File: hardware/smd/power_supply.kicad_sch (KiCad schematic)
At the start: 29 parts, among them T1 Wurth 750370423, U1 LM1117IMPX-3.3, U2 VIPER06, U3 EL3H7, U4 TL431

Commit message: Add capacitor specifications, change capacity around crystal
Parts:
- C10, C2, C6: value 100n 10V -> 100n 10V X7R
- C11: value 100n 35V -> 100n 35V X7R
- C12: value 1n 10V -> 1n 10V X7R
- C13: value 2.2n 35V -> 2.2n 35V X7R
- C7: value 2.2n 50V -> 2.2n 50V X7R
- renumbered C5 to C4, C4 to C5
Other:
- moved on the sheet: C12, C13, C5, C6, R2, R3, R4, U1, U3, U4

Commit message: Drop all tht legacy footprints
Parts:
- C1, C5: footprint KiCadX_Capacitors_THT:CP_Radial_D5.0mm_P1.50mm -> (none)
- C10, C11, C13, C7: footprint Capacitor_THT:C_Disc_D6.0mm_W2.5mm_P5.00mm -> (none)
- C12: footprint Capacitor_THT:C_Disc_D4.3mm_W1.9mm_P5.00mm -> (none)
- C2, C6: footprint Capacitor_THT:C_Disc_D5.0mm_W2.5mm_P5.00mm -> (none)
- C3: footprint Capacitor_THT:C_Rect_L26.5mm_W5.0mm_P22.50mm_MKS4 -> (none)
- D1: footprint Diode_THT:Diode_Bridge_DIP-4_W7.62mm_P5.08mm -> (none)
- D2, D3: footprint Diode_THT:D_DO-41_SOD81_P10.16mm_Horizontal -> (none)
- F1: footprint KiCadX_FuseHolders_THT:FuseHolder_THT_5x20mm_PTF76_RM15mm -> (none)
- R2, R3, R4: footprint Resistor_THT:R_Axial_DIN0207_L6.3mm_D2.5mm_P7.62mm_Horizontal -> (none)
- RV1: footprint Varistor:RV_Disc_D9mm_W3.4mm_P5mm -> (none)
- U1: footprint Package_TO_SOT_SMD:SOT-223-3_TabPin2 -> (none)
- U3: footprint Package_DIP:DIP-4_W7.62mm -> (none)
- U4: footprint Package_TO_SOT_SMD:SOT-23 -> (none)
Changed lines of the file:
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@@
 			)
 		)
-		(property "Footprint" "Capacitor_THT:C_Disc_D5.0mm_W2.5mm_P5.00mm"
+		(property "Footprint" ""
 			(at 113.9952 132.08 0)
 			(effects
@@
 			)
 		)
-		(property "Footprint" "Resistor_THT:R_Axial_DIN0207_L6.3mm_D2.5mm_P7.62mm_Horizontal"
+		(property "Footprint" ""
 			(at 172.72 79.248 90)
 			(effects
@@
 			)
 		)
-		(property "Footprint" "Capacitor_THT:C_Rect_L26.5mm_W5.0mm_P22.50mm_MKS4"
+		(property "Footprint" ""
 			(at 80.9752 66.04 0)
 			(effects
@@
 			)
 		)
-		(property "Footprint" "Resistor_THT:R_Axial_DIN0207_L6.3mm_D2.5mm_P7.62mm_Horizontal"
+		(property "Footprint" ""
 			(at 177.292 88.9 90)
 			(effects
@@
 			)
 		)
-		(property "Footprint" "Capacitor_THT:C_Disc_D5.0mm_W2.5mm_P5.00mm"
+		(property "Footprint" ""
 			(at 60.6552 132.08 0)
 			(effects
@@
 			)
 		)
-		(property "Footprint" "Capacitor_THT:C_Disc_D4.3mm_W1.9mm_P5.00mm"
+		(property "Footprint" ""
 			(at 172.4152 46.99 0)
 			(effects
@@
 			)
 		)
-		(property "Footprint" "Package_TO_SOT_SMD:SOT-223-3_TabPin2"
+		(property "Footprint" ""
 			(at 85.09 124.46 0)
 			(effects
@@
 			)
 		)
-		(property "Footprint" "KiCadX_Capacitors_THT:CP_Radial_D5.0mm_P1.50mm"
+		(property "Footprint" ""
 			(at 97.4852 132.08 0)
 			(effects
@@
 			)
 		)
-		(property "Footprint" "Diode_THT:D_DO-41_SOD81_P10.16mm_Horizontal"
+		(property "Footprint" ""
 			(at 133.35 55.88 0)
 			(effects
@@
 			)
 		)
-		(property "Footprint" "Diode_THT:D_DO-41_SOD81_P10.16mm_Horizontal"
+		(property "Footprint" ""
 			(at 128.27 39.37 0)
 			(effects
@@
 			)
 		)
-		(property "Footprint" "KiCadX_Capacitors_THT:CP_Radial_D5.0mm_P1.50mm"
+		(property "Footprint" ""
 			(at 44.1452 132.08 0)
 			(effects
@@
 			)
 		)
-		(property "Footprint" "Package_TO_SOT_SMD:SOT-23"
+		(property "Footprint" ""
 			(at 172.72 97.536 0)
 			(effects
@@
 			)
 		)
-		(property "Footprint" "Package_DIP:DIP-4_W7.62mm"
+		(property "Footprint" ""
 			(at 163.83 90.17 0)
 			(effects
@@
 			)
 		)
-		(property "Footprint" "Capacitor_THT:C_Disc_D6.0mm_W2.5mm_P5.00mm"
+		(property "Footprint" ""
 			(at 150.8252 46.99 0)
 			(effects
@@
 			)
 		)
-		(property "Footprint" "Capacitor_THT:C_Disc_D6.0mm_W2.5mm_P5.00mm"
+		(property "Footprint" ""
 			(at 133.0452 91.44 0)
 			(effects
@@
 			)
 		)
-		(property "Footprint" "Diode_THT:Diode_Bridge_DIP-4_W7.62mm_P5.08mm"
+		(property "Footprint" ""
 			(at 96.52 73.025 0)
 			(effects
@@
 			)
 		)
-		(property "Footprint" "Resistor_THT:R_Axial_DIN0207_L6.3mm_D2.5mm_P7.62mm_Horizontal"
+		(property "Footprint" ""
 			(at 177.292 81.28 90)
 			(effects
@@
 			)
 		)
-		(property "Footprint" "Capacitor_THT:C_Disc_D6.0mm_W2.5mm_P5.00mm"
+		(property "Footprint" ""
 			(at 172.4152 67.31 0)
 			(effects
@@
 			)
 		)
-		(property "Footprint" "Capacitor_THT:C_Disc_D6.0mm_W2.5mm_P5.00mm"
+		(property "Footprint" ""
 			(at 150.8252 67.31 0)
 			(effects
@@
 			)
 		)
-		(property "Footprint" "Varistor:RV_Disc_D9mm_W3.4mm_P5mm"
+		(property "Footprint" ""
 			(at 47.752 62.23 90)
 			(effects
@@
 			)
 		)
-		(property "Footprint" "KiCadX_FuseHolders_THT:FuseHolder_THT_5x20mm_PTF76_RM15mm"
+		(property "Footprint" ""
 			(at 43.18 57.658 90)
 			(effects

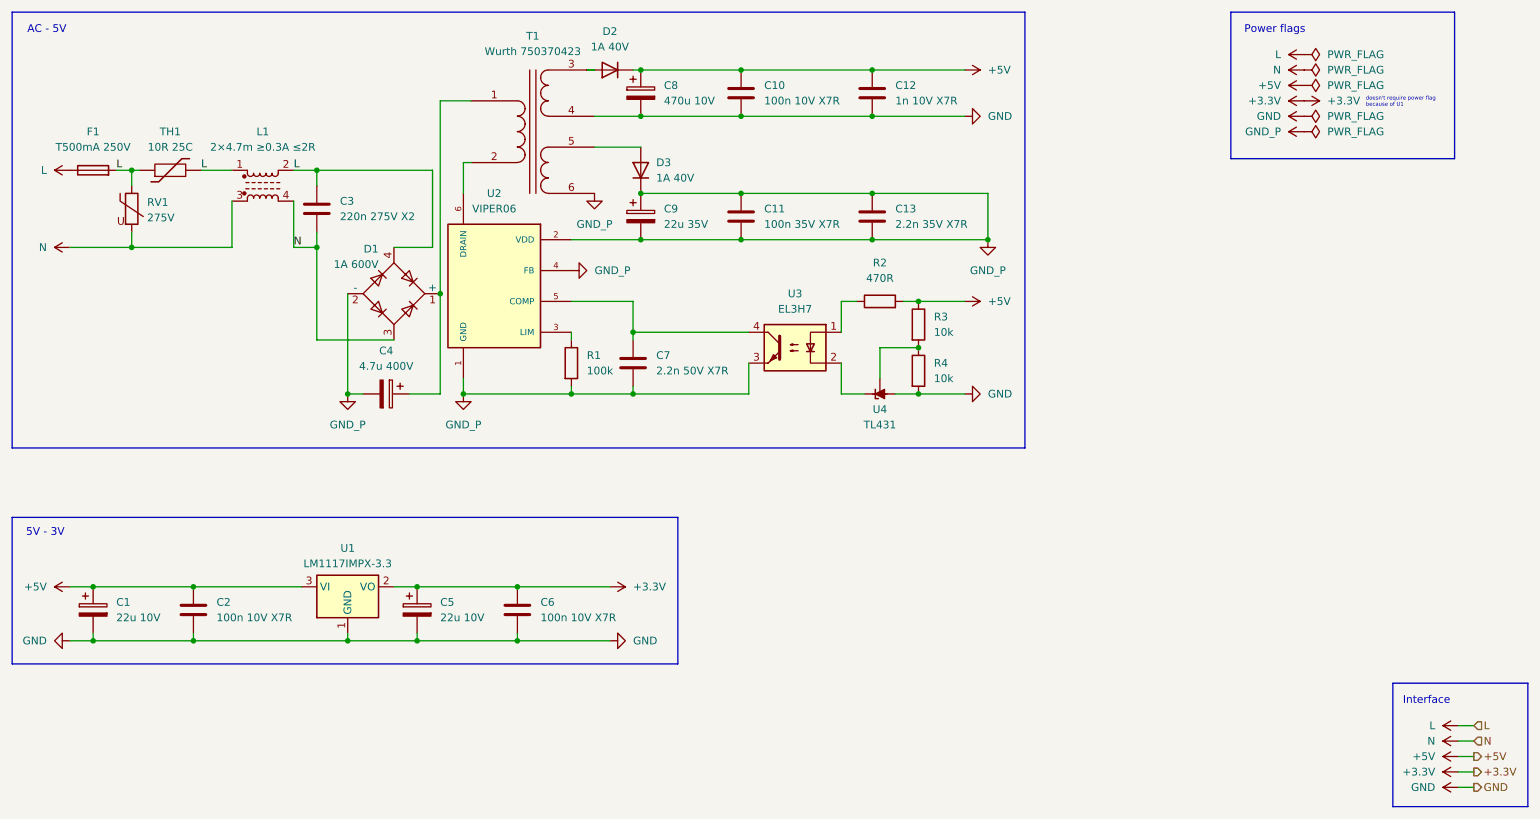
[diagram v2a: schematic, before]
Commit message: Assign footprints and JLC numbers (plus minor changes)
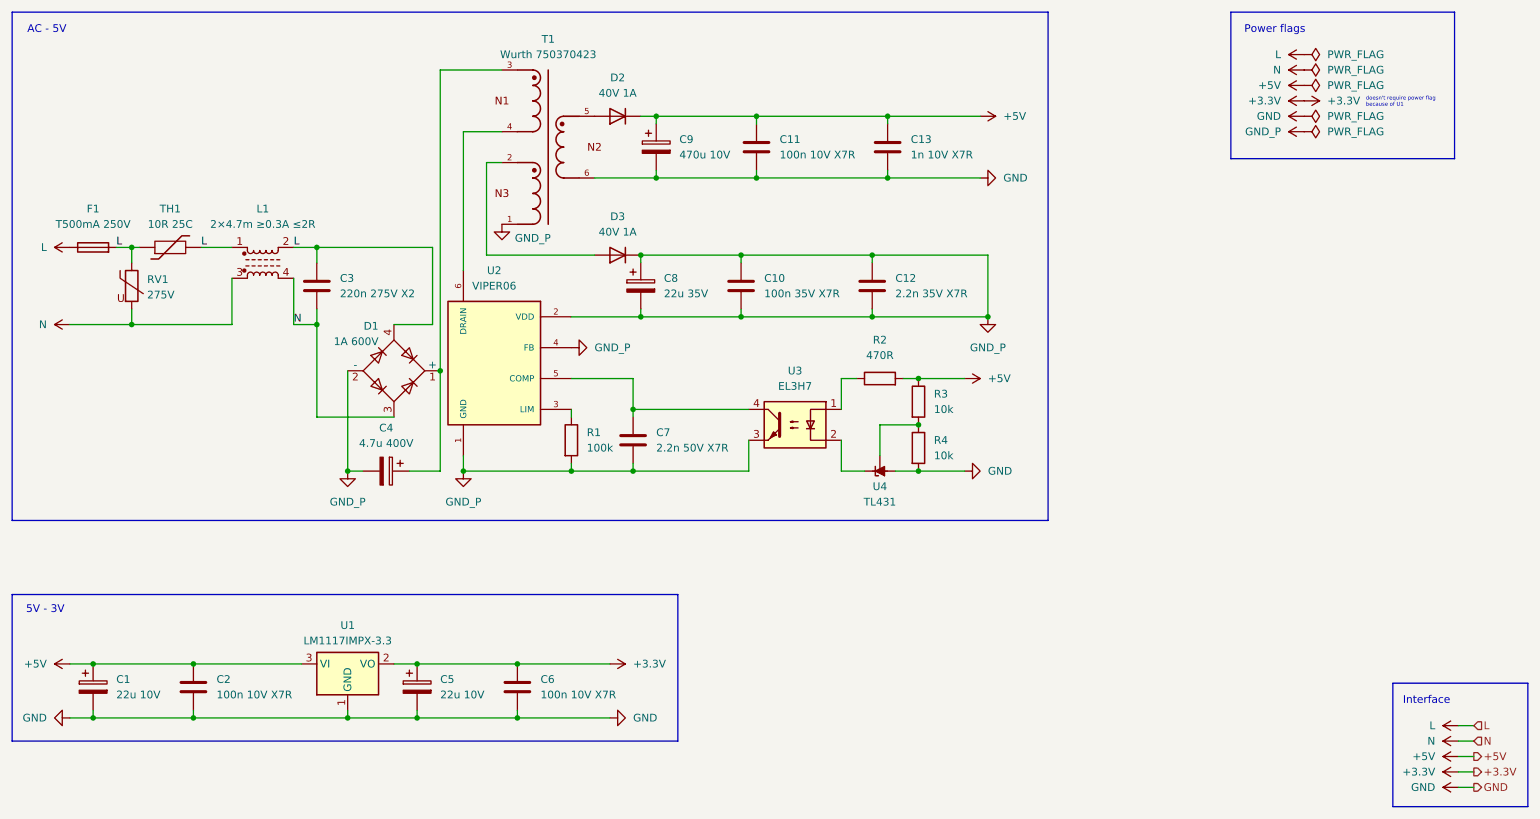
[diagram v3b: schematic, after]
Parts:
- removed T1: Wurth 750370423, symbol Device:Transformer_1P_2S
- added T1: Wurth 750370423, KiCadX_Transformers_THT:Wurth_750370423_THT_E13, symbol KiCadX_Transformers:Wurth_750370423
- C1, C5: footprint (none) -> Capacitor_SMD:CP_Elec_5x5.4; JLCPCB (none) -> C22387966
- C10: renamed from C11; footprint (none) -> Capacitor_SMD:C_0603_1608Metric; JLCPCB (none) -> C14663
- C11: renamed from C10; footprint (none) -> Capacitor_SMD:C_0402_1005Metric; JLCPCB (none) -> C309458
- C12: renamed from C13; footprint (none) -> Capacitor_SMD:C_0402_1005Metric; JLCPCB (none) -> C106861
- C13: renamed from C12; footprint (none) -> Capacitor_SMD:C_0402_1005Metric; JLCPCB (none) -> C541372
- C2, C6: footprint (none) -> Capacitor_SMD:C_0402_1005Metric; JLCPCB (none) -> C309458
- C3: footprint (none) -> Capacitor_THT:C_Rect_L13.0mm_W6.0mm_P10.00mm_FKS3_FKP3_MKS4; JLCPCB (none) -> C489075
- C4: footprint (none) -> Capacitor_SMD:CP_Elec_10x10.5; JLCPCB (none) -> C88703
- C7: footprint (none) -> Capacitor_SMD:C_0402_1005Metric; JLCPCB (none) -> C106861
- C8: renamed from C9; footprint (none) -> Capacitor_SMD:CP_Elec_5x5.4; JLCPCB (none) -> C239256
- C9: renamed from C8; footprint (none) -> Capacitor_SMD:CP_Elec_6.3x7.7; JLCPCB (none) -> C2858856
- D1: footprint (none) -> Package_TO_SOT_SMD:TO-269AA; JLCPCB (none) -> C2487
- D2, D3: value 1A 40V -> 40V 1A; footprint (none) -> Diode_SMD:D_SOD-323; JLCPCB (none) -> C191023
- F1: footprint (none) -> KiCadX_Fuse_SMD:Fuse_2410_6125Metric_6.1x2.5mm; JLCPCB (none) -> C136377
- L1: footprint (none) -> Inductor_THT:Choke_Schaffner_RN112-04-17.7x17.1mm; JLCPCB (none) -> C6660027
- R1: footprint (none) -> Resistor_SMD:R_0402_1005Metric; JLCPCB (none) -> C25741
- R2: footprint (none) -> Resistor_SMD:R_0402_1005Metric; JLCPCB (none) -> C25117
- R3, R4: footprint (none) -> Resistor_SMD:R_0402_1005Metric; JLCPCB (none) -> C25744
- RV1: footprint (none) -> Varistor:RV_Disc_D9mm_W4.4mm_P5mm; JLCPCB (none) -> C125493
- TH1: footprint (none) -> KiCadX_Thermistors_THT:NTC10D_7_Disc_D7.0mm_P5.0mm; JLCPCB (none) -> C332360
- U1: footprint (none) -> Package_TO_SOT_SMD:SOT-223; JLCPCB (none) -> C23984
- U2: footprint (none) -> KiCadX_ACDC_Converters_SMD:VIPER06_SSO10; JLCPCB (none) -> C501111
- U3: footprint (none) -> Package_SO:SSOP-4_4.4x2.6mm_P1.27mm; JLCPCB (none) -> C92243
- U4: footprint (none) -> Package_TO_SOT_SMD:SOT-23; JLCPCB (none) -> C41283
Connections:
- net GND: now also T1.6
- net GND_P: now also T1.1
- net at C4.1, D1.1 (+): now also T1.3
- net at U2.10 (DRAIN), U2.6 (DRAIN), U2.7 (DRAIN)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: now also T1.4
- net at D2.2 (A): now also T1.5
- net at D3.2 (A): now also T1.2
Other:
- moved on the sheet: C1, C10, C11, C12, C13, C2, C3, C4, C5, C6, C7, C8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

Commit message: Complete PCB and schematics after fucking a lot of iterations
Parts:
- removed L1: 2×4.7m ≥0.3A ≤2R, Inductor_THT:Choke_Schaffner_RN112-04-17.7x17.1mm, symbol Device:L_Ferrite_Coupled
- removed U1: LM1117IMPX-3.3, Package_TO_SOT_SMD:SOT-223, symbol Regulator_Linear:LM1117MP-3.3
- added FL1: 2×4.7m ≥0.3A ≤2R, KiCadX_Inductors_THT:TDK_B82720K_Vertical_13x9.5mm_P10x7.5mm, symbol Device:Filter_EMI_LL_1423
- added U1: LM1117F-3.3, Package_TO_SOT_SMD:SOT-89-3, symbol Regulator_Linear:AZ1117-3.3
- C1, C5: footprint Capacitor_SMD:CP_Elec_5x5.4 -> Capacitor_THT:CP_Radial_D4.0mm_P1.50mm; JLCPCB C22387966 -> C43800
- C4: footprint Capacitor_SMD:CP_Elec_10x10.5 -> Capacitor_THT:CP_Radial_D6.3mm_P2.50mm; JLCPCB C88703 -> C2931505
- C8: renamed from C9; footprint Capacitor_SMD:CP_Elec_6.3x7.7 -> KiCadX_Capacitors_THT:CP_Radial_D6.0mm_P2.50mm; JLCPCB C2858856 -> C7499930
- C9: renamed from C8; footprint Capacitor_SMD:CP_Elec_5x5.4 -> Capacitor_THT:CP_Radial_D5.0mm_P2.00mm; JLCPCB C239256 -> C43346
- F1: footprint KiCadX_Fuse_SMD:Fuse_2410_6125Metric_6.1x2.5mm -> Fuse_Littelfuse_395Series; JLCPCB C136377 -> C2762401
- R1: value 100k -> 30k; JLCPCB C25741 -> C138008
- T1: JLCPCB 750370423 -> C27978219
- renumbered C11 to C10, C10 to C11, C13 to C12, C12 to C13, D3 to D2, D2 to D3
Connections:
- net +3.3V: now also U1.2 (VO)
- net +5V: now also U1.3 (VI)
- net GND: now also T1.8, U1.1 (GND); no longer T1.6
- net GND_P: no longer C11.1, C13.1, C9.1, D2.1 (K), U2.2 (VDD)
- net L: now also FL1.1, FL1.4
- net N: now also FL1.2, FL1.3
- net VRECT: now reaches C4.1, D1.1 (+), T1.3
- net DRAIN: now reaches T1.4, U2.10 (DRAIN), U2.6 (DRAIN), U2.7 (DRAIN), U2.8 (DRAIN), U2.9 (DRAIN)
- new net: C11.1, C13.1, C9.1, D2.1 (K), U2.2 (VDD)
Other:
- moved on the sheet: C11, C13, C9, D2

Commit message: Rename JLCPCB property to LCSC PN across schematic files
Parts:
- C1, C5: JLCPCB C43800 -> (none); LCSC PN (none) -> C43800
- C10, C2, C6: JLCPCB C309458 -> (none); LCSC PN (none) -> C309458
- C11: JLCPCB C14663 -> (none); LCSC PN (none) -> C14663
- C12: JLCPCB C541372 -> (none); LCSC PN (none) -> C541372
- C13, C7: JLCPCB C106861 -> (none); LCSC PN (none) -> C106861
- C3: JLCPCB C489075 -> (none); LCSC PN (none) -> C489075
- C4: JLCPCB C2931505 -> (none); LCSC PN (none) -> C2931505
- C8: JLCPCB C7499930 -> (none); LCSC PN (none) -> C7499930
- C9: JLCPCB C43346 -> (none); LCSC PN (none) -> C43346
- D1: JLCPCB C2487 -> (none); LCSC PN (none) -> C2487
- D2, D3: JLCPCB C191023 -> (none); LCSC PN (none) -> C191023
- F1: JLCPCB C2762401 -> (none); LCSC PN (none) -> C2762401
- FL1: JLCPCB C125597 -> (none); LCSC PN (none) -> C125597
- R1: JLCPCB C138008 -> (none); LCSC PN (none) -> C138008
- R2: JLCPCB C25117 -> (none); LCSC PN (none) -> C25117
- R3, R4: JLCPCB C25744 -> (none); LCSC PN (none) -> C25744
- RV1: JLCPCB C125493 -> (none); LCSC PN (none) -> C125493
- T1: JLCPCB C27978219 -> (none); LCSC PN (none) -> C27978219
- TH1: JLCPCB C332360 -> (none); LCSC PN (none) -> C332360
- U1: JLCPCB C126019 -> (none); LCSC PN (none) -> C126019
- U2: JLCPCB C501111 -> (none); LCSC PN (none) -> C501111
- U3: JLCPCB C92243 -> (none); LCSC PN (none) -> C92243
- U4: JLCPCB C41283 -> (none); LCSC PN (none) -> C41283
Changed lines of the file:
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@@
 			)
 		)
-		(property "JLCPCB" "C138008"
+		(property "LCSC PN" "C138008"
 			(at 121.92 100.33 0)
 			(effects
@@
 			)
 		)
-		(property "JLCPCB" "C309458"
+		(property "LCSC PN" "C309458"
 			(at 113.03 140.97 0)
 			(effects
@@
 			)
 		)
-		(property "JLCPCB" "C2931505"
-			(at 91.44 105.41 0)
+		(property "LCSC PN" "C2931505"
+			(at 91.44 105.41 90)
 			(effects
 				(font
@@
 			)
 		)
-		(property "JLCPCB" "C25117"
-			(at 172.72 90.17 0)
+		(property "LCSC PN" "C25117"
+			(at 172.72 90.17 90)
 			(effects
 				(font
@@
 			)
 		)
-		(property "JLCPCB" "C489075"
+		(property "LCSC PN" "C489075"
 			(at 80.01 74.93 0)
 			(effects
@@
 			)
 		)
-		(property "JLCPCB" "C25744"
+		(property "LCSC PN" "C25744"
 			(at 179.07 101.6 0)
 			(effects
@@
 			)
 		)
-		(property "JLCPCB" "C309458"
+		(property "LCSC PN" "C309458"
 			(at 59.69 140.97 0)
 			(effects
@@
 			)
 		)
-		(property "JLCPCB" "C43346"
+		(property "LCSC PN" "C43346"
 			(at 135.89 74.93 0)
 			(effects
@@
 			)
 		)
-		(property "JLCPCB" "C501111"
+		(property "LCSC PN" "C501111"
 			(at 109.22 87.63 0)
 			(effects
@@
 			)
 		)
-		(property "JLCPCB" "C541372"
+		(property "LCSC PN" "C541372"
 			(at 173.99 52.07 0)
 			(effects
@@
 			)
 		)
-		(property "JLCPCB" "C43800"
+		(property "LCSC PN" "C43800"
 			(at 96.52 140.97 0)
 			(effects
@@
 			)
 		)
-		(property "JLCPCB" "C27978219"
+		(property "LCSC PN" "C27978219"
 			(at 118.11 52.07 0)
 			(effects
@@
 			)
 		)
-		(property "JLCPCB" "C191023"
+		(property "LCSC PN" "C191023"
 			(at 123.19 69.85 0)
 			(effects
@@
 			)
 		)
-		(property "JLCPCB" "C191023"
+		(property "LCSC PN" "C191023"
 			(at 129.54 46.99 0)
 			(effects
@@
 			)
 		)
-		(property "JLCPCB" "C43800"
+		(property "LCSC PN" "C43800"
 			(at 43.18 140.97 0)
 			(effects
@@
 			)
 		)
-		(property "JLCPCB" "C41283"
+		(property "LCSC PN" "C41283"
 			(at 172.72 105.41 0)
 			(effects
@@
 			)
 		)
-		(property "JLCPCB" "C332360"
-			(at 55.88 68.58 0)
+		(property "LCSC PN" "C332360"
+			(at 55.88 68.58 90)
 			(effects
 				(font
@@
 			)
 		)
-		(property "JLCPCB" "C92243"
+		(property "LCSC PN" "C92243"
 			(at 158.75 97.79 0)
 			(effects
@@
 			)
 		)
-		(property "JLCPCB" "C309458"
+		(property "LCSC PN" "C309458"
 			(at 152.4 52.07 0)
 			(effects
@@
 			)
 		)
-		(property "JLCPCB" "C7499930"
+		(property "LCSC PN" "C7499930"
 			(at 135.89 52.07 0)
 			(effects
@@
 			)
 		)
-		(property "JLCPCB" "C106861"
+		(property "LCSC PN" "C106861"
 			(at 132.08 100.33 0)
 			(effects
@@
 			)
 		)
-		(property "JLCPCB" "C2487"
+		(property "LCSC PN" "C2487"
 			(at 92.71 88.9 0)
 			(effects
@@
 			)
 		)
-		(property "JLCPCB" "C126019"
+		(property "LCSC PN" "C126019"
 			(at 85.09 137.16 0)
 			(effects
@@
 			)
 		)
-		(property "JLCPCB" "C125597"
+		(property "LCSC PN" "C125597"
 			(at 71.12 71.12 0)
 			(effects
@@
 			)
 		)
-		(property "JLCPCB" "C25744"
+		(property "LCSC PN" "C25744"
 			(at 179.07 93.98 0)
 			(effects
@@
 			)
 		)
-		(property "JLCPCB" "C106861"
+		(property "LCSC PN" "C106861"
 			(at 173.99 74.93 0)
 			(effects
@@
 			)
 		)
-		(property "JLCPCB" "C14663"
+		(property "LCSC PN" "C14663"
 			(at 152.4 74.93 0)
 			(effects
@@
 			)
 		)
-		(property "JLCPCB" "C125493"
+		(property "LCSC PN" "C125493"
 			(at 49.53 74.93 0)
 			(effects
@@
 			)
 		)
-		(property "JLCPCB" "C2762401"
-			(at 43.18 68.58 0)
+		(property "LCSC PN" "C2762401"
+			(at 43.18 68.58 90)
 			(effects
 				(font

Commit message: Update library paths from KiCadX to PCM_SKC
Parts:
- T1: symbol KiCadX_Transformers:Wurth_750370423 -> PCM_SKC_Transformers:Wurth_750370423
- U2: symbol KiCadX_ACDC_Converters:VIPER06 -> PCM_SKC_ACDC_Converters:VIPER06
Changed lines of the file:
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@@
 	)
 	(symbol
-		(lib_id "KiCadX_ACDC_Converters:VIPER06")
+		(lib_id "PCM_SKC_ACDC_Converters:VIPER06")
 		(at 109.22 87.63 0)
 		(mirror y)
@@
 	(symbol
 		(lib_name "Wurth_750370423_1")
-		(lib_id "KiCadX_Transformers:Wurth_750370423")
+		(lib_id "PCM_SKC_Transformers:Wurth_750370423")
 		(at 118.11 52.07 0)
 		(unit 1)

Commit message: Relink symbols and footprints to new lib and fix few errors
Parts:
- C8: footprint KiCadX_Capacitors_THT:CP_Radial_D6.0mm_P2.50mm -> PCM_SKC_Capacitors_THT:CP_Radial_D6.0mm_P2.50mm
- F1: footprint Fuse_Littelfuse_395Series -> Fuse:Fuse_Littelfuse_395Series
- FL1: footprint KiCadX_Inductors_THT:TDK_B82720K_Vertical_13x9.5mm_P10x7.5mm -> PCM_SKC_Inductors_THT:TDK_B82720K_Vertical_13x9.5mm_P10x7.5mm
- T1: footprint KiCadX_Transformers_THT:Wurth_750370423_THT_E13 -> PCM_SKC_Transformers_THT:Wurth_750370423_THT_E13
- TH1: footprint KiCadX_Thermistors_THT:NTC10D_7_Disc_D7.0mm_P5.0mm -> PCM_SKC_Thermistors_THT:NTC10D_7_Disc_D7.0mm_P5.0mm
- U2: footprint KiCadX_ACDC_Converters_SMD:VIPER06_SSO10 -> PCM_SKC_ACDC_Converters_SMD:STMicroelectronics_VIPER06_SSO10
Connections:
- net AUX: now reaches C11.1, C13.1, C9.1, D2.1 (K), U2.2 (VDD)
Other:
- note added: "doesn't require power flag because of T1"

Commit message: Make vias a bit bigger because of JLCPCB prices and change out-of-stock component
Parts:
- F1: LCSC PN C2762401 -> C354902
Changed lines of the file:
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@@
 			)
 		)
-		(property "LCSC PN" "C2762401"
+		(property "LCSC PN" "C354902"
 			(at 43.18 68.58 90)
 			(effects
